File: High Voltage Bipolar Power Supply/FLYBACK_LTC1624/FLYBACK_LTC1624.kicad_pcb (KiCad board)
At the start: 2 copper layers, 100 x 60 mm, 81 parts, among them J1 1715721, J2 Conn_01x02, J3 1715734, Q1 PZT2222A, Q2 IRL540NS, Q3 TIP125, Q4 TIP120, T1 VP3-0138, U1 LTC1624CS8, U2 TSR_1-2450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

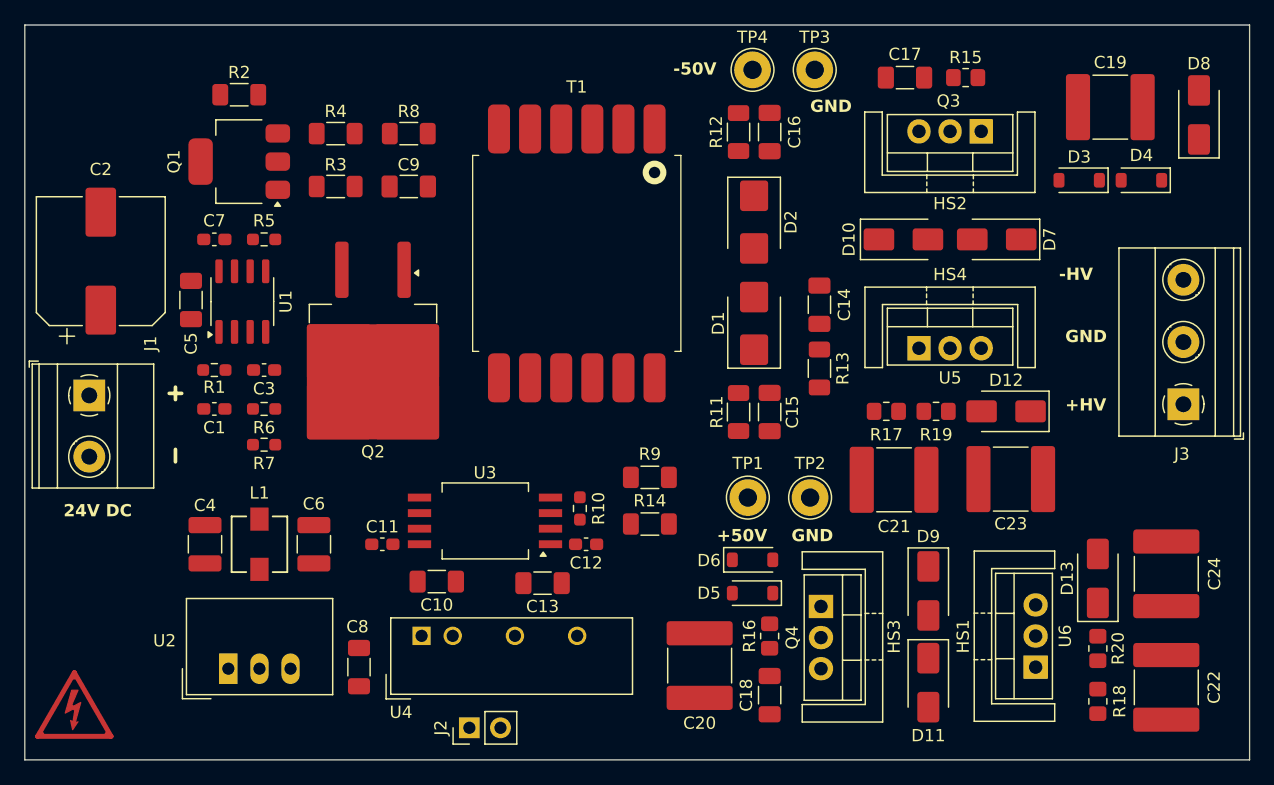
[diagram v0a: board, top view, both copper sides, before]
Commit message: FLYBACK_LTC1624 : Design failed, can't buy LM377HV for -50V
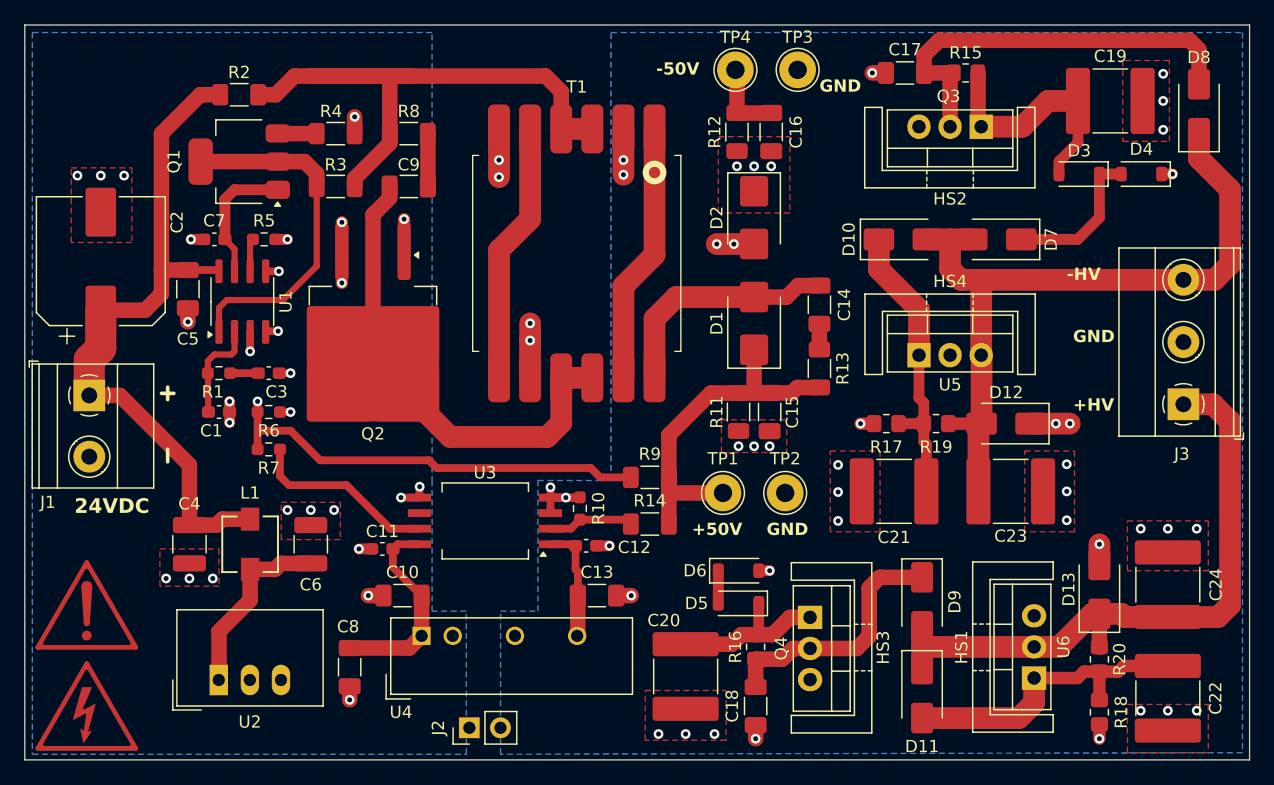
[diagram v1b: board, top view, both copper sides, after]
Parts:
- removed REF**: Symbol_HighVoltage_Triangle_6x6mm_Copper, Symbol:Symbol_HighVoltage_Triangle_6x6mm_Copper
- added SYM1: SYM_Flash_Large, Symbol:Symbol_Attention_Triangle_8x7mm_Copper, F.Cu at (107.1, 117.3)
- added SYM2: SYM_Flash_Large, Symbol:Symbol_HighVoltage_Triangle_8x7mm_Copper, F.Cu at (107.1, 125.6)
- moved C13 4.56 mm to (148.7, 116.6), turned to 0 degrees
- moved C10 3.02 mm to (132.8, 116.6), turned to 180 degrees
- moved TP1 2.07 mm to (159.0, 108.2)
- moved TP2 2.07 mm to (164.1, 108.2)
- moved Q2 1.46 mm to (130.4, 96.2)
- moved C18 1.45 mm to (161.7, 125.6)
- moved C20 1.45 mm to (156.0, 123.2)
- moved D6 1.45 mm to (160.3, 114.6)
- moved R16 1.45 mm to (161.7, 120.8)
- moved D5 1.41 mm to (160.3, 117.2)
- moved TP3 1.40 mm to (165.1, 73.7)
- moved TP4 1.40 mm to (160.0, 73.7)
- moved C4 1.27 mm to (115.4, 112.4)
- moved Q4 1.26 mm to (166.1, 118.4)
- moved HS3 1.26 mm to (171.0, 120.8)
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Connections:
- R10 pad 1: GNDS -> GND
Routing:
- net -50V: track 0.00 -> 92.0 mm, vias 0 -> 2
- net +50V: track 0.00 -> 70.3 mm
- net -44V: track 0.00 -> 61.6 mm
- net +24V: track 0.00 -> 57.2 mm
- net +44V: track 0.00 -> 52.4 mm
- net Net-(R2-Pad2): track 0.00 -> 52.2 mm
- net Net-(U1-SET): track 0.00 -> 41.9 mm, vias 0 -> 2
- net Net-(Q2-D): track 0.00 -> 35.8 mm
- net +5V: track 0.00 -> 31.3 mm
- net Net-(D2-A): track 0.00 -> 30.5 mm, vias 0 -> 4
- net Net-(Q1-C): track 0.00 -> 28.8 mm
- net Net-(D11-A): track 0.00 -> 25.3 mm
- net Net-(D10-K): track 0.00 -> 24.3 mm
- net GND: track 0.00 -> 24.2 mm, vias 0 -> 39
- net Net-(T1-Pad5): track 0.00 -> 21.4 mm
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- added copper zone on B.Cu, net GND
- added copper zone on F.Cu, net GND
- added copper zone on In1.Cu, net GND
- added copper zone on B.Cu, net GNDS
- added copper zone on F.Cu, net GNDS
- added copper zone on In1.Cu, net GNDS
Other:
- copper layers 2 -> 4
- board text added: "24VDC"
- board text removed: "24V DC"
